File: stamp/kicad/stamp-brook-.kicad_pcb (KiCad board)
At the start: 2 copper layers, 96.2 x 45.2 mm, 17 parts, among them J10 Conn_01x02_Female, J2 Conn_01x05_Male, J3 Screw_Terminal_01x20, J4 Conn_01x04_Female, J5 Conn_01x05_Male, J6 Conn_01x04_Female, J7 Conn_01x04_Male, J8 Conn_01x04_Male, J9 Conn_02x10_Odd_Even, U1 RP2040_Stamp

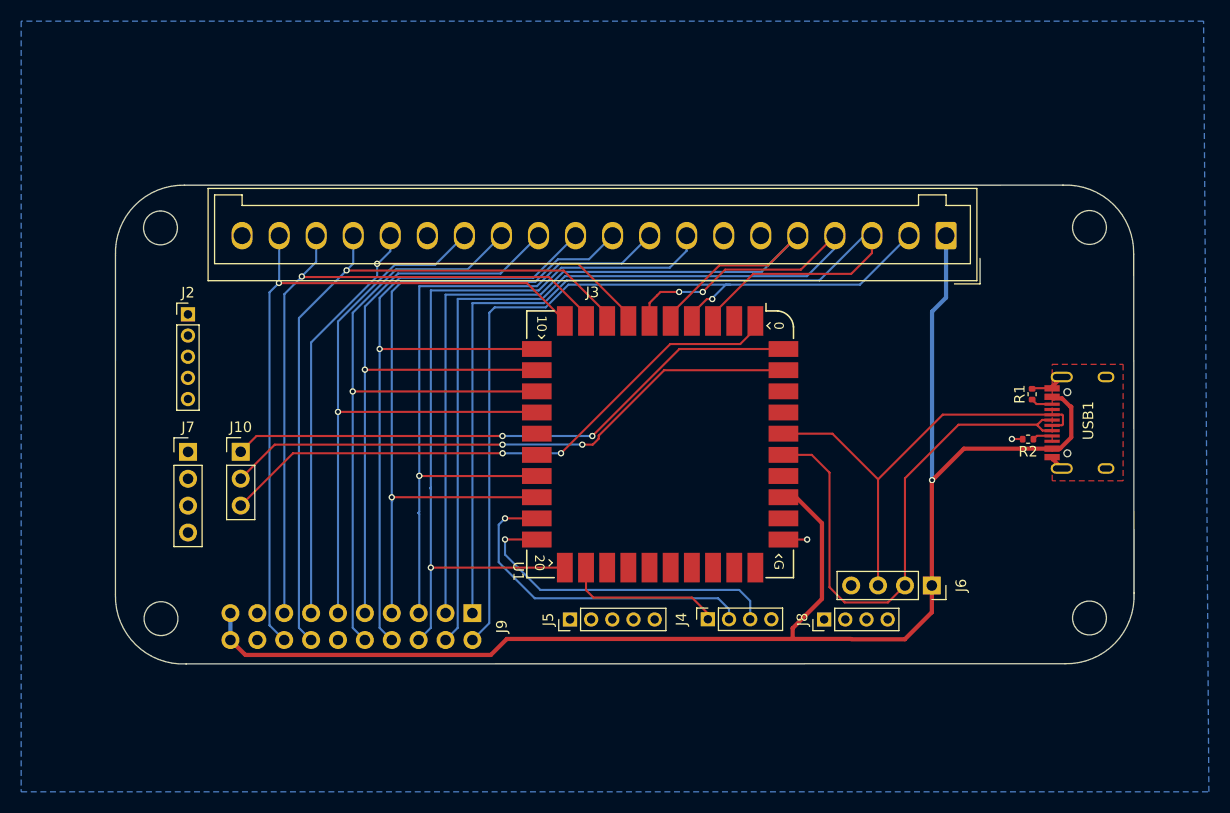
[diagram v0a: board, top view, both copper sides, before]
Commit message: Add Turbo pins, OLED pins, and LS/DP/RS pins. Change Resistors to larger component
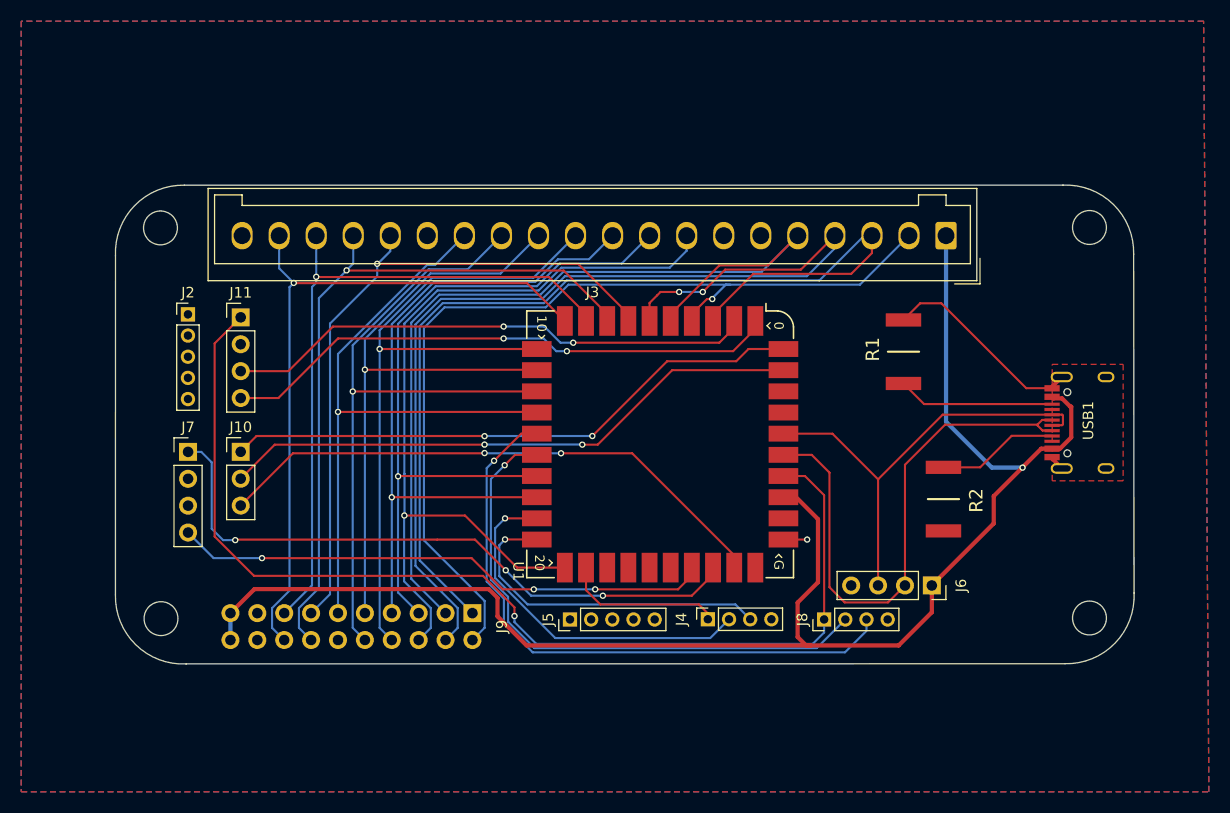
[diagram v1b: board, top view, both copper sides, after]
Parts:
- added J11: Conn_01x04_Female, Connector_PinHeader_2.54mm:PinHeader_1x04_P2.54mm_Vertical, F.Cu at (107.6, 66.1)
- R1, R2: footprint Resistor_SMD:R_0402_1005Metric -> CRCW25125K10JNTG:RESC6332X70N
- moved R1 12.8 mm to (170.2, 69.3)
- moved R2 9.80 mm to (174.0, 83.2), turned to -90 degrees
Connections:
- J7 pad 1: unconnected-(J7-Pad1) -> LS
- J7 pad 2: unconnected-(J7-Pad2) -> GND
- J7 pad 3: unconnected-(J7-Pad3) -> GND
- J7 pad 4: unconnected-(J7-Pad4) -> RS
- J8 pad 1: unconnected-(J8-Pad1) -> 3.3V
- J8 pad 2: unconnected-(J8-Pad2) -> TURBO LED
- J8 pad 3: unconnected-(J8-Pad3) -> TURBO
- J8 pad 4: unconnected-(J8-Pad4) -> GND
- U1 pad 1: RGB DATA -> OLED SDA
- U1 pad 15: unconnected-(U1-Pad15) -> TURBO
- U1 pad 16: unconnected-(U1-Pad16) -> TURBO LED
- U1 pad 2: unconnected-(U1-Pad2) -> OLED SCL
- U1 pad 27: unconnected-(U1-Pad27) -> RS
- U1 pad 28: unconnected-(U1-Pad28) -> LS
- U1 pad 29: unconnected-(U1-Pad29) -> RGB DATA
- U1 pad 34: unconnected-(U1-Pad34) -> 3.3V
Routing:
- net 3.3V: track 0.00 -> 102.3 mm, vias 0 -> 1
- net LS: track 0.00 -> 60.4 mm, vias 0 -> 3
- net TURBO: track 0.00 -> 58.7 mm, vias 0 -> 1
- net TURBO LED: track 0.00 -> 53.4 mm, vias 0 -> 1
- net OLED SDA: track 0.00 -> 53.1 mm, vias 0 -> 2
- net RS: track 0.00 -> 51.1 mm, vias 0 -> 3
- net OLED SCL: track 0.00 -> 50.2 mm, vias 0 -> 2
- net GND: track 7.99 -> 23.1 mm, vias 2 -> 1
- net Net-(USB1-Pad10): track 2.08 -> 14.9 mm
- net Net-(R2-Pad1): track 1.91 -> 11.5 mm
- net DOWN: track 79.7 -> 87.2 mm
- net HOME: track 73.4 -> 79.6 mm
- net UP: track 89.4 -> 95.1 mm
- net LEFT: track 93.3 -> 97.6 mm
- net RIGHT: track 81.4 -> 84.4 mm
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
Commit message: Minor adjustments to traces, remove J2 and J5 due to nonuse
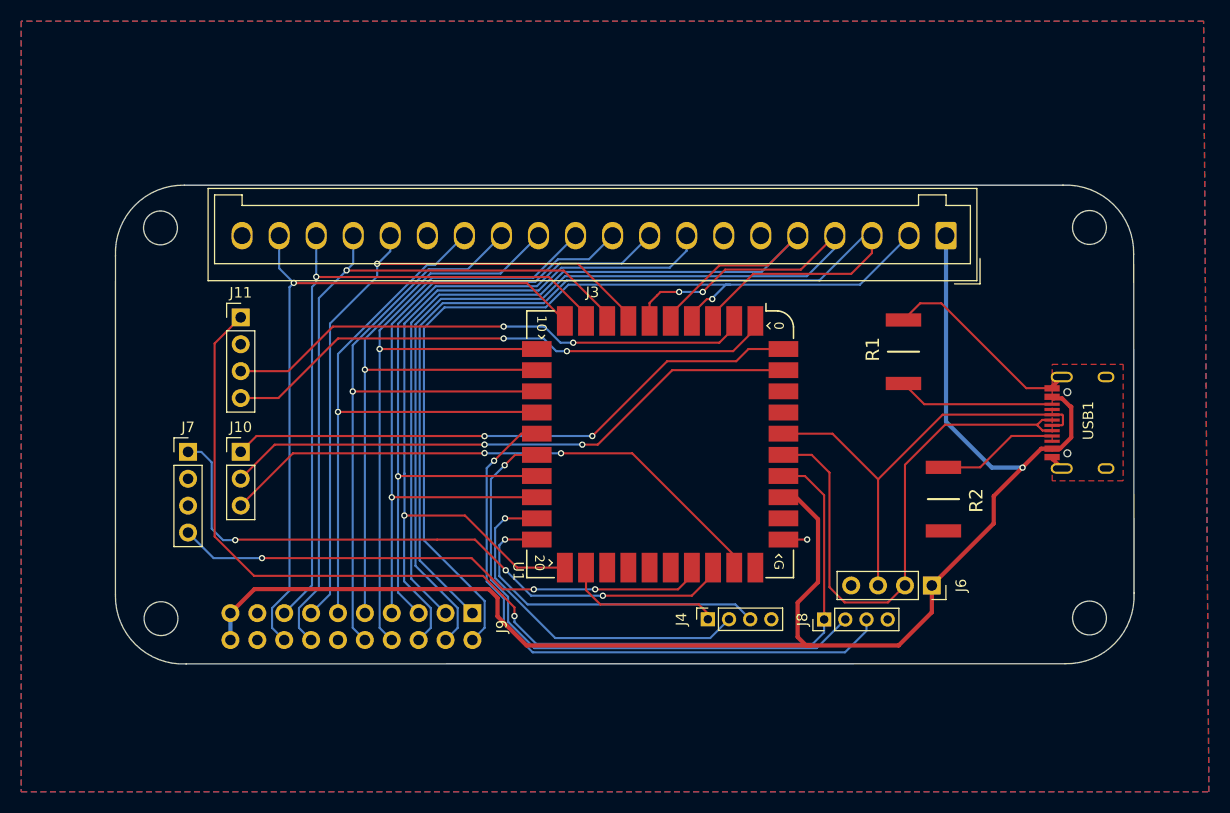
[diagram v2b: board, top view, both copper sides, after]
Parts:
- removed J2, J5: Conn_01x05_Male, Connector_PinHeader_2.00mm:PinHeader_1x05_P2.00mm_Vertical
